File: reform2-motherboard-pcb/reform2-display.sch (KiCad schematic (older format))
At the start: 38 parts, among them J24 EDP_HEADER, U10 SN65DSI86IPAPQ1

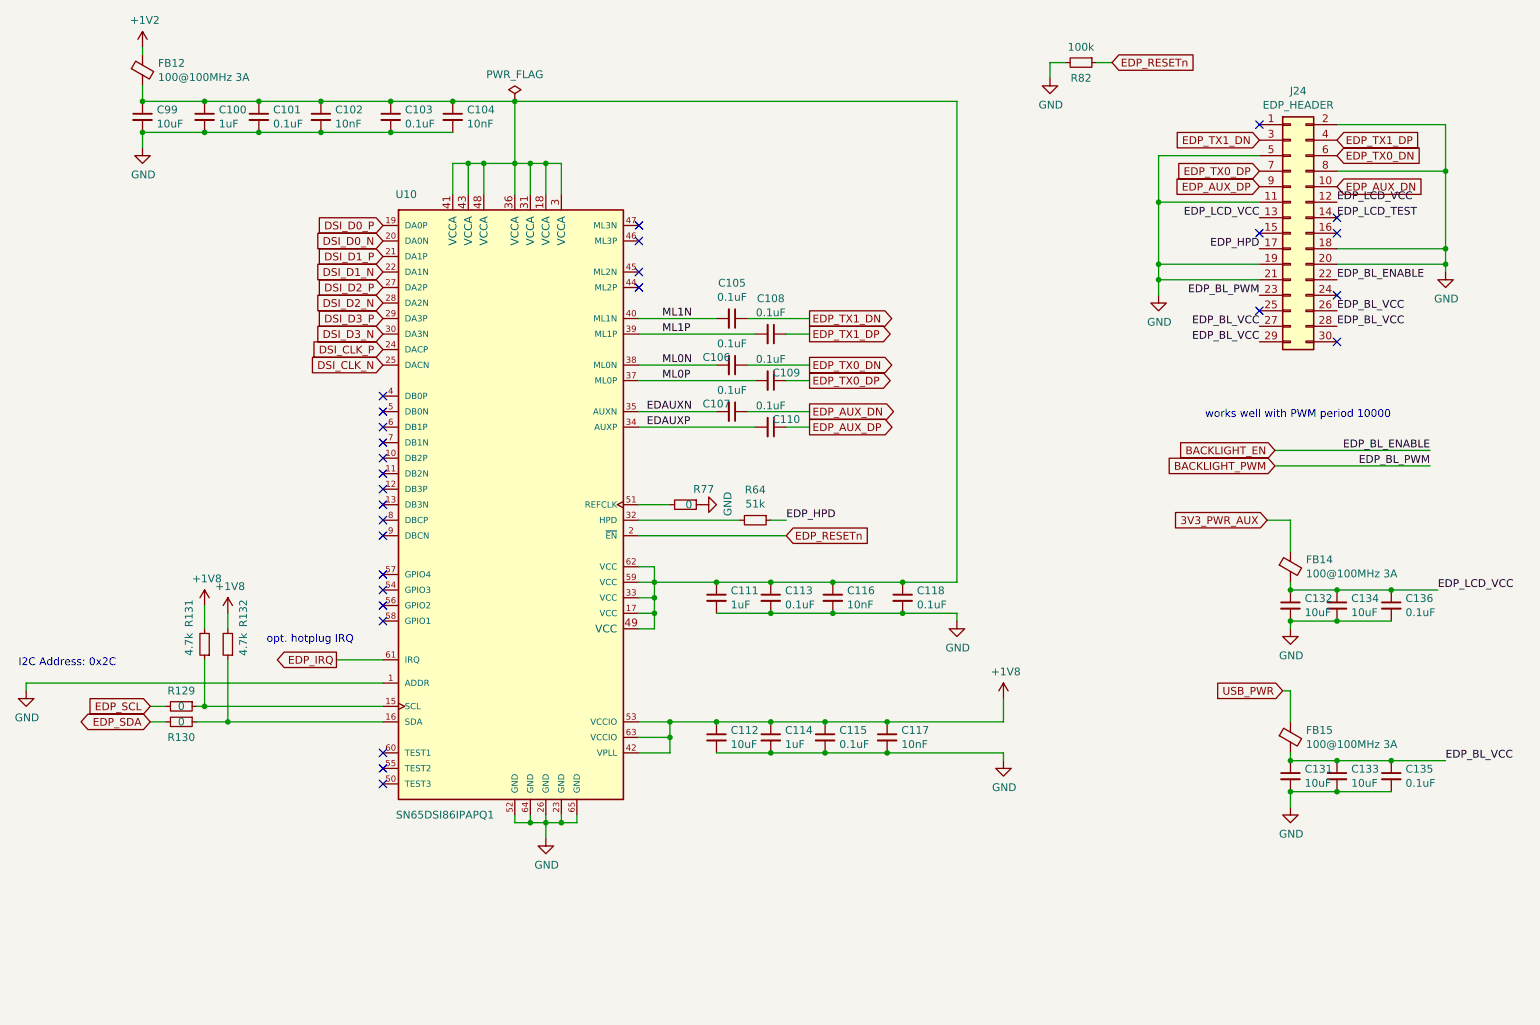
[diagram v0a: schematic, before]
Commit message: motherboard: add the split-up and cleaned up schematics that were made for the book
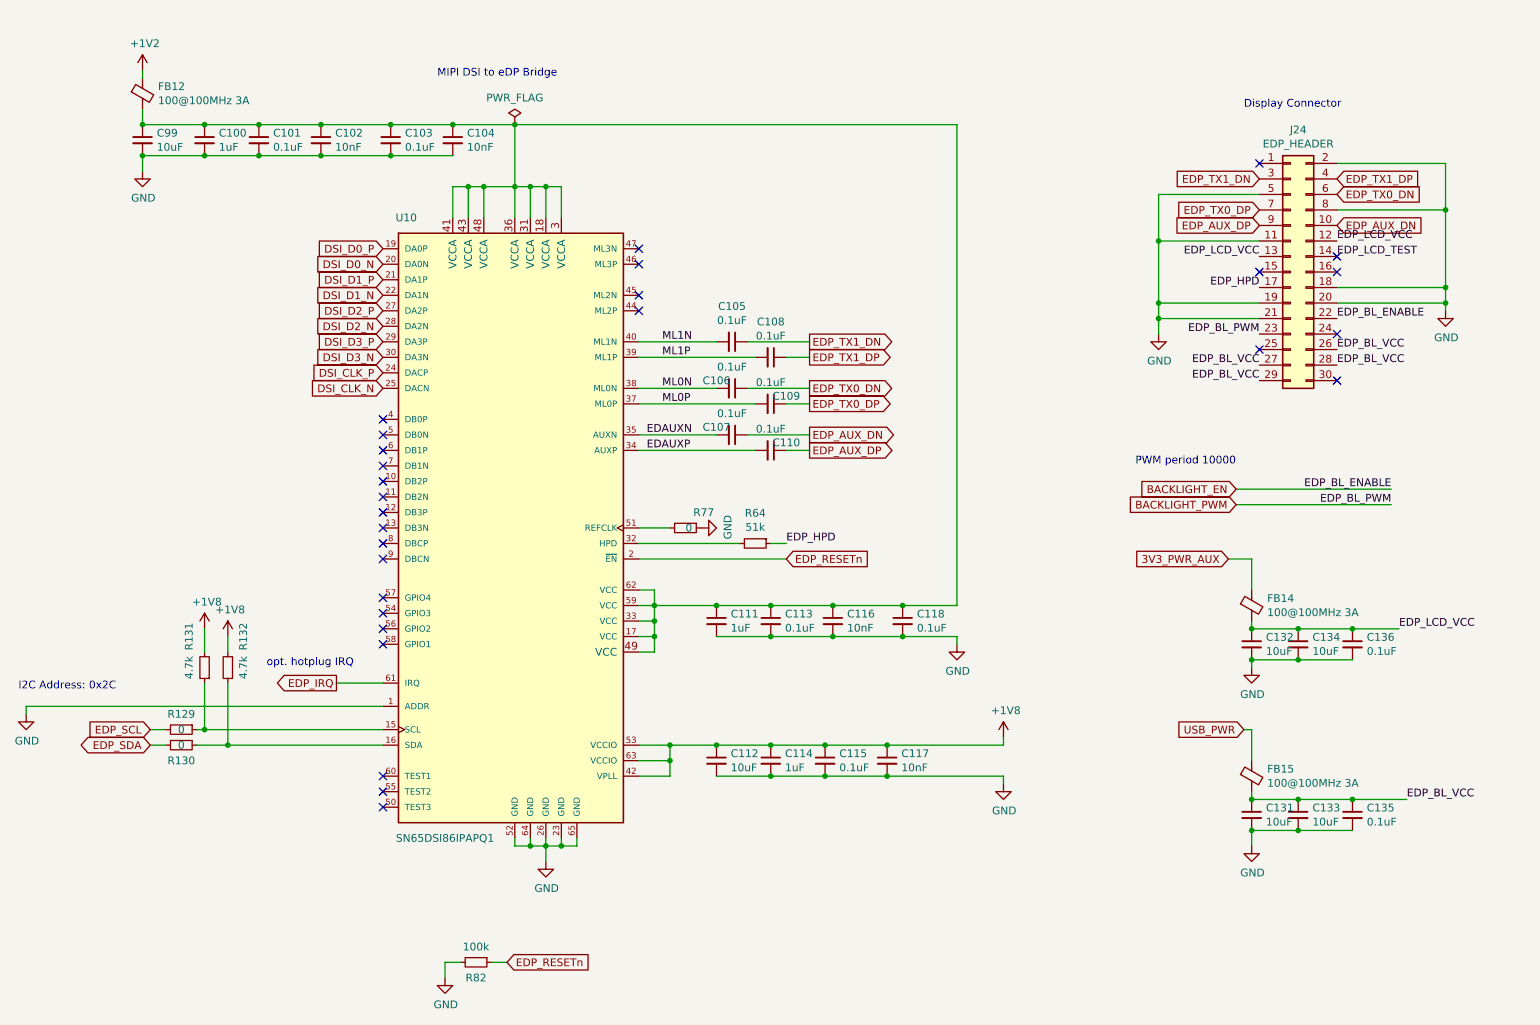
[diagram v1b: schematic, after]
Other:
- note added: "Display Connector"
- note added: "MIPI DSI to eDP Bridge"
- note added: "PWM period 10000"
- note removed: "works well with PWM period 10000"
- moved on the sheet: C100, C101, C102, C103, C104, C105, C106, C107, C108, C109, C110, C111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
